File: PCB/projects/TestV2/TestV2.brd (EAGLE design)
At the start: 100 x 100 mm, 129 parts, among them U1 38kHz, U2 38kHz, X1 USB-MINIB

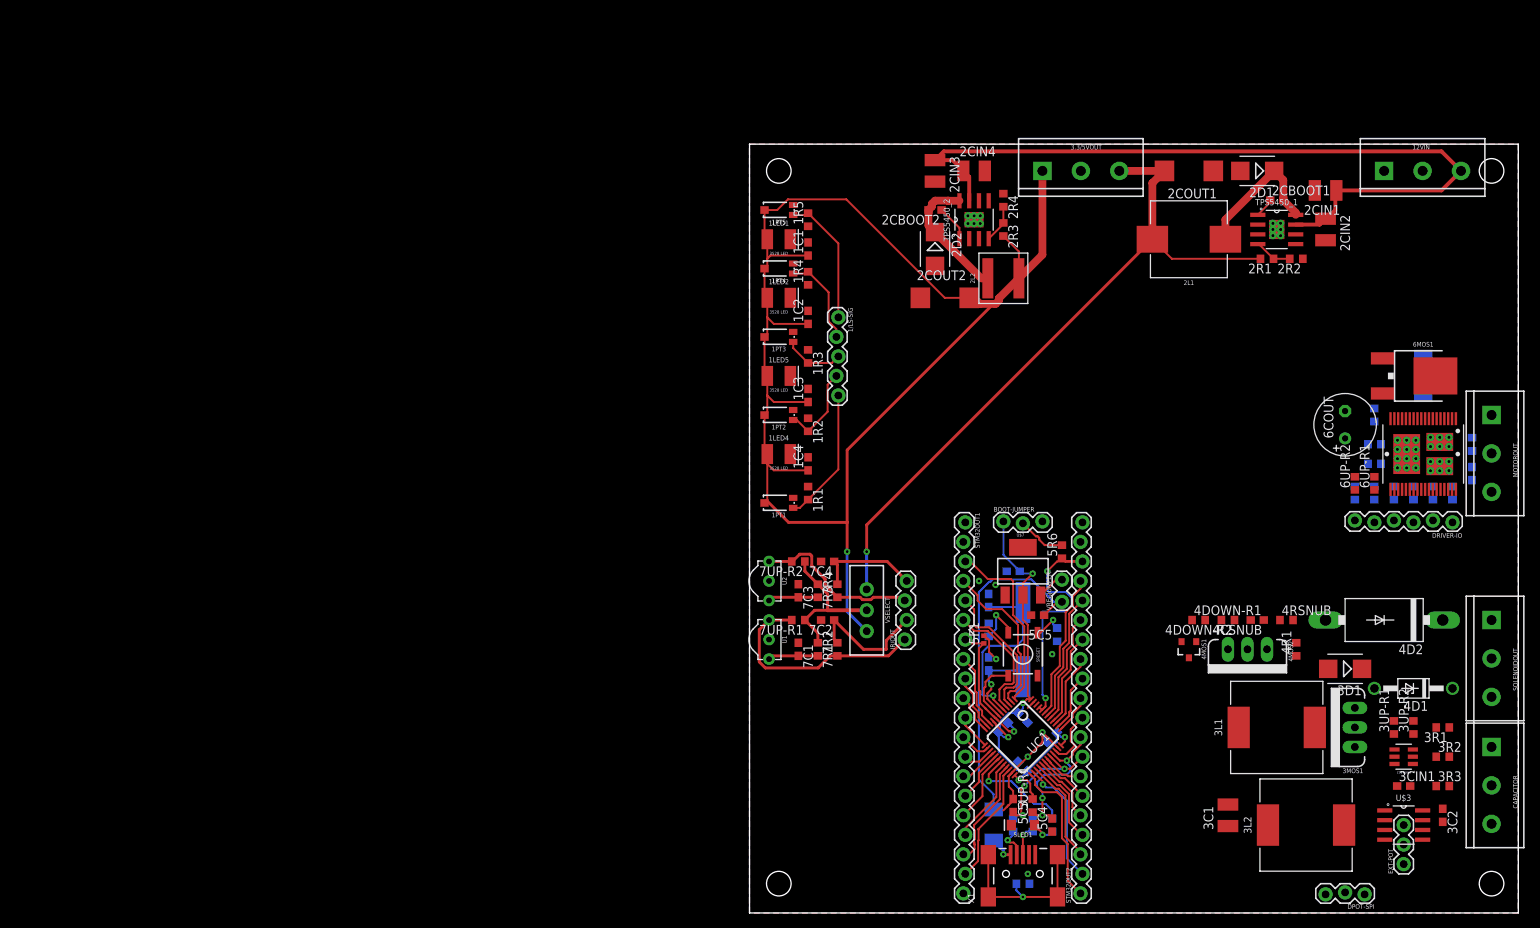
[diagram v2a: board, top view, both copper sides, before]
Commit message: 16/12 PCB shit too much happened shld have committed more often but wtv deleted stm32 sheet added IR and mouse sensor Finally routed everything, gerber files are included hopefully done for now
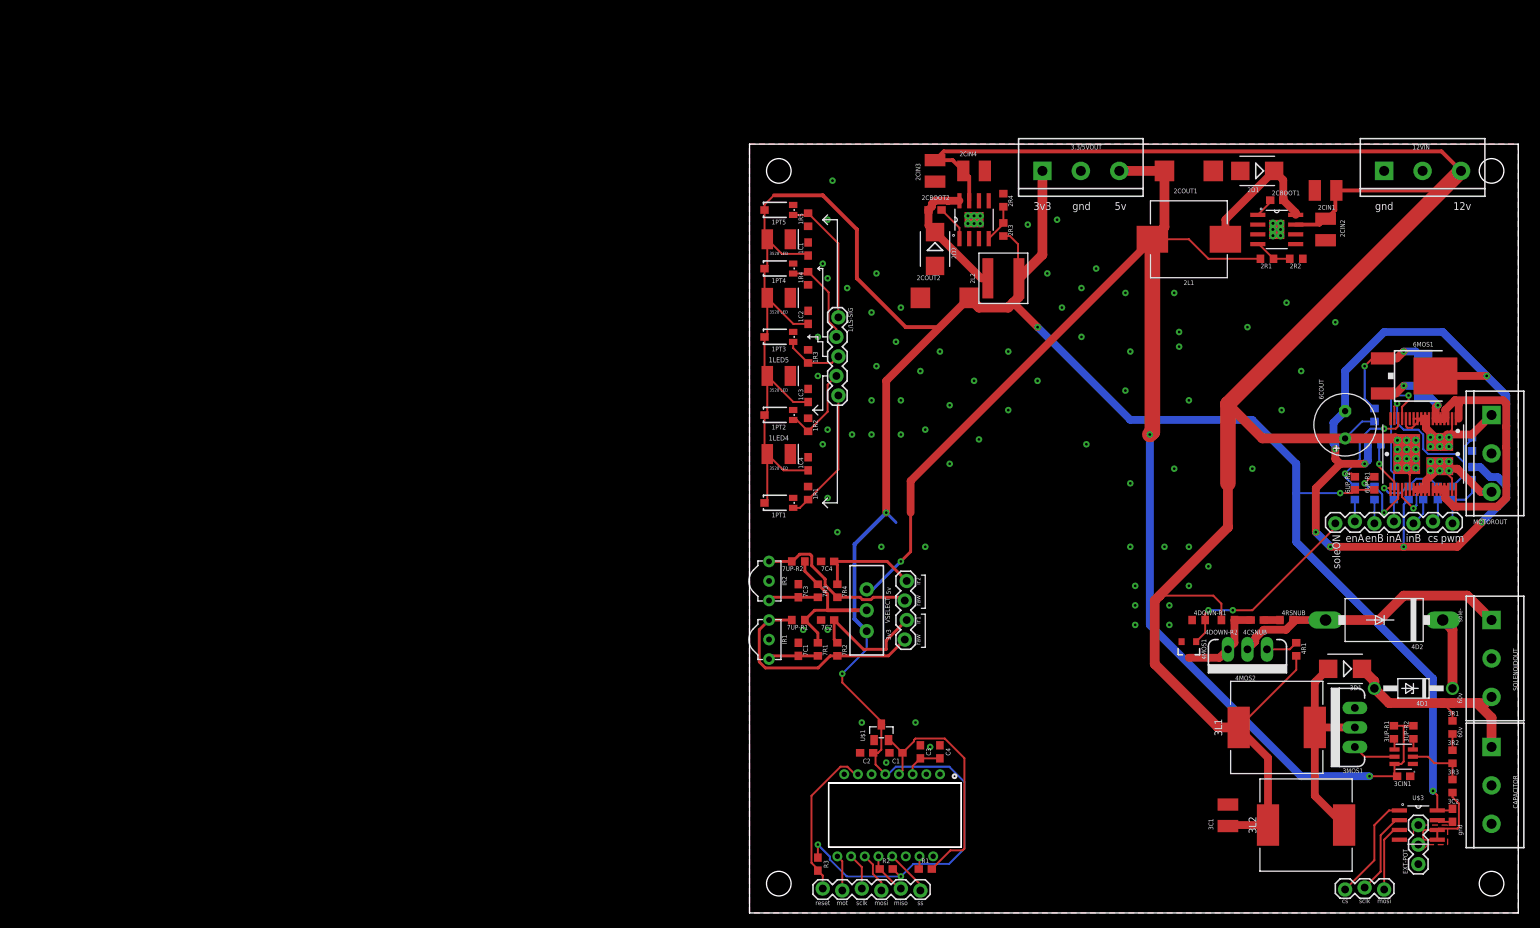
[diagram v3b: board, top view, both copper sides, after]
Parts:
- removed 5C1, 5C2: 18pF, rcl:C0603
- removed 5C10, 5C5, 5C7, 5C8, 5C9: 1uF, rcl:C0603
- removed 5C3, 5C4: 47pF, rcl:C0603
- removed 5C6: 1uf, rcl:C0603
- removed 5D1: SS14, diode:DO-214AC
- removed 5DOWN-R1, 5R3, 5R4: 22, rcl:R0603
- removed 5F1: 300ohm bead, rcl:R0402
- removed 5LED1: RED, SparkFun-LED:LED-1206
- removed 5OSC: 8MHz, SparkFun-Clocks:HC49UP
- removed 5R1, 5R5: 1k, rcl:R0603
- removed 5R2, 5R6: 10k, rcl:R0603
- removed 5RESET: TAC_SWITCHSMD, SparkFun-Retired:TACTILE-SWITCH-SMD
- removed 5UP-R1: 1.5k, rcl:R0603
- removed BOOT-JUMPER: (no value), SparkFun-Connectors:1X03_LOCK
- removed STM32OUT1, STM32OUT2: (no value), SparkFun-Connectors:1X20_LOCK
- removed U$7: AMS1117-3.3, SparkFun-IC-Power:SOT223
- removed UC1: STM32F103CBT6, stm32:LQFP48
- removed VREGJUMPER: (no value), SparkFun-Connectors:1X02_LOCK
- removed X1: USB-MINIB, SparkFun-Connectors:USB-MINIB
- added C1, C2: 1.0uF, SparkFun-Capacitors:0603
- added C3: 0.1uF, SparkFun-Capacitors:0603
- added C4: 4.7uF, SparkFun-Capacitors:0603
- added J1: (no value), SparkFun-Connectors:1X06_LOCK
- added R1: 39, SparkFun-Resistors:0603
- added R2, R3: 10k, SparkFun-Resistors:0603
- added U$1: LN6206, MCP1700T-3302E_TT:SOT95P237X112-3N
- added U$2: PMW3360, JH:PMW3360
- DRIVER-IO: device SparkFun-Connectors:1X06_LOCK -> SparkFun-Connectors:1X07_LOCK
- moved 6DOWN-R1 5.85 mm to (85.7, 54.6), turned to 270 degrees
- moved DPOT-SPI 2.62 mm to (82.5, 3.17)
- moved EXT-POT 1.91 mm to (87.0, 6.35)
- moved U$3 1.91 mm to (87.0, 11.4)
- moved 3CIN1 1.27 mm to (85.1, 17.8)
- moved 3C2 1.27 mm to (91.4, 12.7)
- moved 3R1 1.27 mm to (91.4, 24.1), turned to 90 degrees
- moved 3R2 1.27 mm to (91.4, 20.3), turned to 90 degrees
- moved 3R3 1.27 mm to (91.4, 16.5), turned to 90 degrees
- moved 6R4 1.27 mm to (87.6, 54.6)
- moved 3UP-R1 0.63 mm to (83.8, 23.5)
- moved 3UP-R2 0.63 mm to (86.4, 23.5)
- moved 6R5 0.63 mm to (89.5, 54.6)
- renumbered U1 to IR1, U2 to IR2
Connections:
- removed net 0: STM32OUT1.19, UC1.22
- removed net 1: STM32OUT1.18, UC1.21
- removed net 10: STM32OUT1.9, UC1.11
- removed net 11: STM32OUT1.8, UC1.10
- removed net 12: STM32OUT1.6, UC1.4
- removed net 13: STM32OUT1.5, UC1.3
- removed net 14: STM32OUT1.4, UC1.2
- removed net 15: STM32OUT2.17, UC1.43
- removed net 16: STM32OUT2.16, UC1.42
- removed net 17: STM32OUT2.15, UC1.41
- removed net 18: STM32OUT2.14, UC1.40
- removed net 19: STM32OUT2.13, UC1.39
- removed net 2: STM32OUT1.17, UC1.20
- removed net 20: STM32OUT2.12, UC1.38
- removed net 21: STM32OUT2.11, UC1.37
- removed net 22: STM32OUT2.10, UC1.34
- removed net 23_USBDP: 5C4.2, 5R4.1, 5UP-R1.1, STM32OUT2.9, UC1.33
- removed net 24_USBDM: 5C3.2, 5R3.1, STM32OUT2.8, UC1.32
- removed net 25: STM32OUT2.7, UC1.31
- removed net 26: STM32OUT2.6, UC1.30
- removed net 27: STM32OUT2.5, UC1.29
- removed net 28: STM32OUT2.4, UC1.28
- removed net 29: STM32OUT2.3, UC1.27
- removed net 3: STM32OUT1.16, UC1.18
- removed net 30: STM32OUT2.2, UC1.26
- removed net 31: STM32OUT2.1, UC1.25
- removed net 32: 5R6.1, STM32OUT2.18, UC1.44, UC1.45
- removed net 4: STM32OUT1.15, UC1.17
- removed net 5: STM32OUT1.14, UC1.16
- removed net 6: STM32OUT1.13, UC1.15
- removed net 7: STM32OUT1.12, UC1.14
- removed net 8: STM32OUT1.11, UC1.13
- removed net 9: STM32OUT1.10, UC1.12
- removed net AGND: 5C10.2, 5F1.1, STM32OUT1.7, UC1.8
- removed net DISC: UC1.46
- removed net N$18: U$7.3, VREGJUMPER.2
- removed net N$27: 5R1.2, 5RESET.1, 5RESET.2
- removed net N$28: 5LED1.A, 5R5.1
- removed net N$30: 5R6.2, BOOT-JUMPER.2
- removed net N$31: 5R5.2, UC1.19
- removed net N$59: 5R3.2, X1.D-
- removed net N$60: 5R4.2, X1.D+
- removed net OSC_IN: 5C2.1, 5OSC.2, UC1.5
- removed net OSC_OUT: 5C1.1, 5OSC.1, UC1.6
- removed net RESET: 5R2.1, 5RESET.3, 5RESET.4, UC1.7
- removed net VBAT: STM32OUT1.3, UC1.1
- removed net V_USB: 5D1.A, X1.VBUS
- new net 1.8V: C1.1, R1.2, U$1.2, U$2.P4
- new net N$40: J1.6, U$2.P13
- new net N$42: J1.5, R2.1, U$2.P12
- new net N$45: J1.4, U$2.P11
- new net N$46: J1.3, U$2.P10
- new net N$47: J1.2, U$2.P9
- new net N$48: C3.2, C4.2, U$2.P3
- new net NRESET: J1.1, R3.2, U$2.P7
- net 3.3V: now also C2.1, R2.2, R3.1, U$1.3, U$2.P5; no longer 5C10.1, 5C6.1, 5C7.1, 5C8.1, 5C9.1, 5R2.2, 5UP-R1.2, BOOT-JUMPER.1, U$7.2, UC1.24, UC1.36, UC1.48, UC1.9
- net 5V: no longer 5C5.1, 5D1.C, VREGJUMPER.1
- net GND: now also C1.2, C2.2, C3.1, C4.1, U$1.1, U$2.P8; no longer 5C1.2, 5C2.2, 5C3.1, 5C4.1, 5C5.2, 5C6.2, 5C7.2, 5C8.2, 5C9.2, 5DOWN-R1.1, 5F1.2, 5LED1.C, 5R1.1, BOOT-JUMPER.3, U$7.1, UC1.23, UC1.35, UC1.47, X1.GND
- net N$36: now also R1.1, U$2.P15; no longer 5DOWN-R1.2, X1.S1, X1.S2, X1.S3, X1.S4
- net SOLENOIDON: now also DRIVER-IO.7
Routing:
- net 12V: track 104.2 -> 293.5 mm
- net 3.3V: track 249.0 -> 369.8 mm, vias 6 -> 7
- net GND: track 22.7 -> 117.8 mm, vias 7 -> 79
- net 5V: track 136.3 -> 192.8 mm, vias 1 -> 3
- net N$19: track 0.00 -> 54.2 mm, vias 0 -> 2
- net SOLENOID-: track 0.00 -> 36.6 mm
- net 32: track 32.8 -> 0.00 mm, vias 2 -> 0
- net 1.8V: track 0.00 -> 32.6 mm
- net VCC_1: track 0.00 -> 28.9 mm
- net N$32: track 0.00 -> 28.6 mm
- net N$11: track 0.00 -> 27.8 mm
- net SOLENOIDON: track 0.00 -> 26.2 mm, vias 0 -> 2
- net N$33: track 0.00 -> 26.1 mm
- net OSC_IN: track 24.8 -> 0.00 mm, vias 1 -> 0
- net N$16: track 0.00 -> 24.2 mm, vias 0 -> 1
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- added copper zone on layer 1, net N$10
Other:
- outline, holes or cut-outs redrawn
- board text added: "12v"
- board text added: "3v3"
- board text added: "5v"
- board text added: "60v"
- board text added: "cs"
- board text added: "enA"
- board text added: "enB"
- board text added: "gnd"
- board text added: "inA"
- board text added: "inB"
- board text added: "ir1"
- board text added: "ir2"
- board text added: "miso"
- board text added: "mosi"
- board text added: "mot"
- board text added: "pwm"
- board text added: "raw"
- board text added: "reset"
- board text added: "sclk"
- board text added: "sole-"
- board text added: "soleON"
- board text added: "ss"
